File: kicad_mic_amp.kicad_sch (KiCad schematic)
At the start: 0 parts

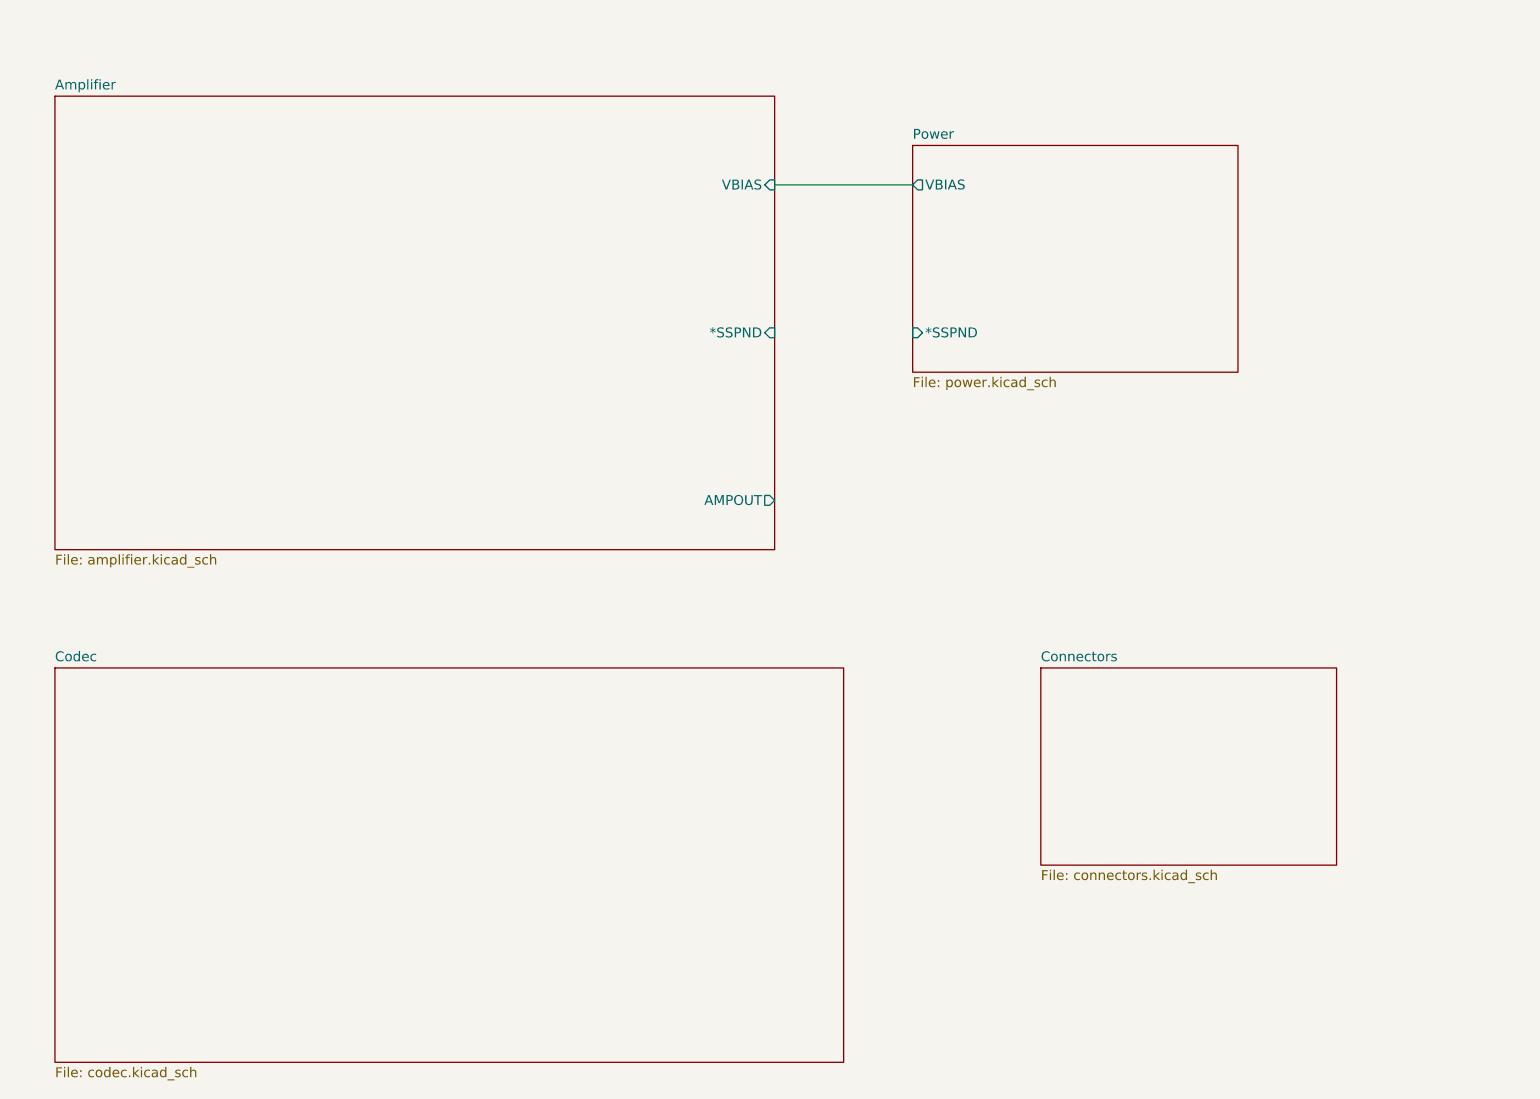
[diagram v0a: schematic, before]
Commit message: Added Connectors; added hierarchical labels connections
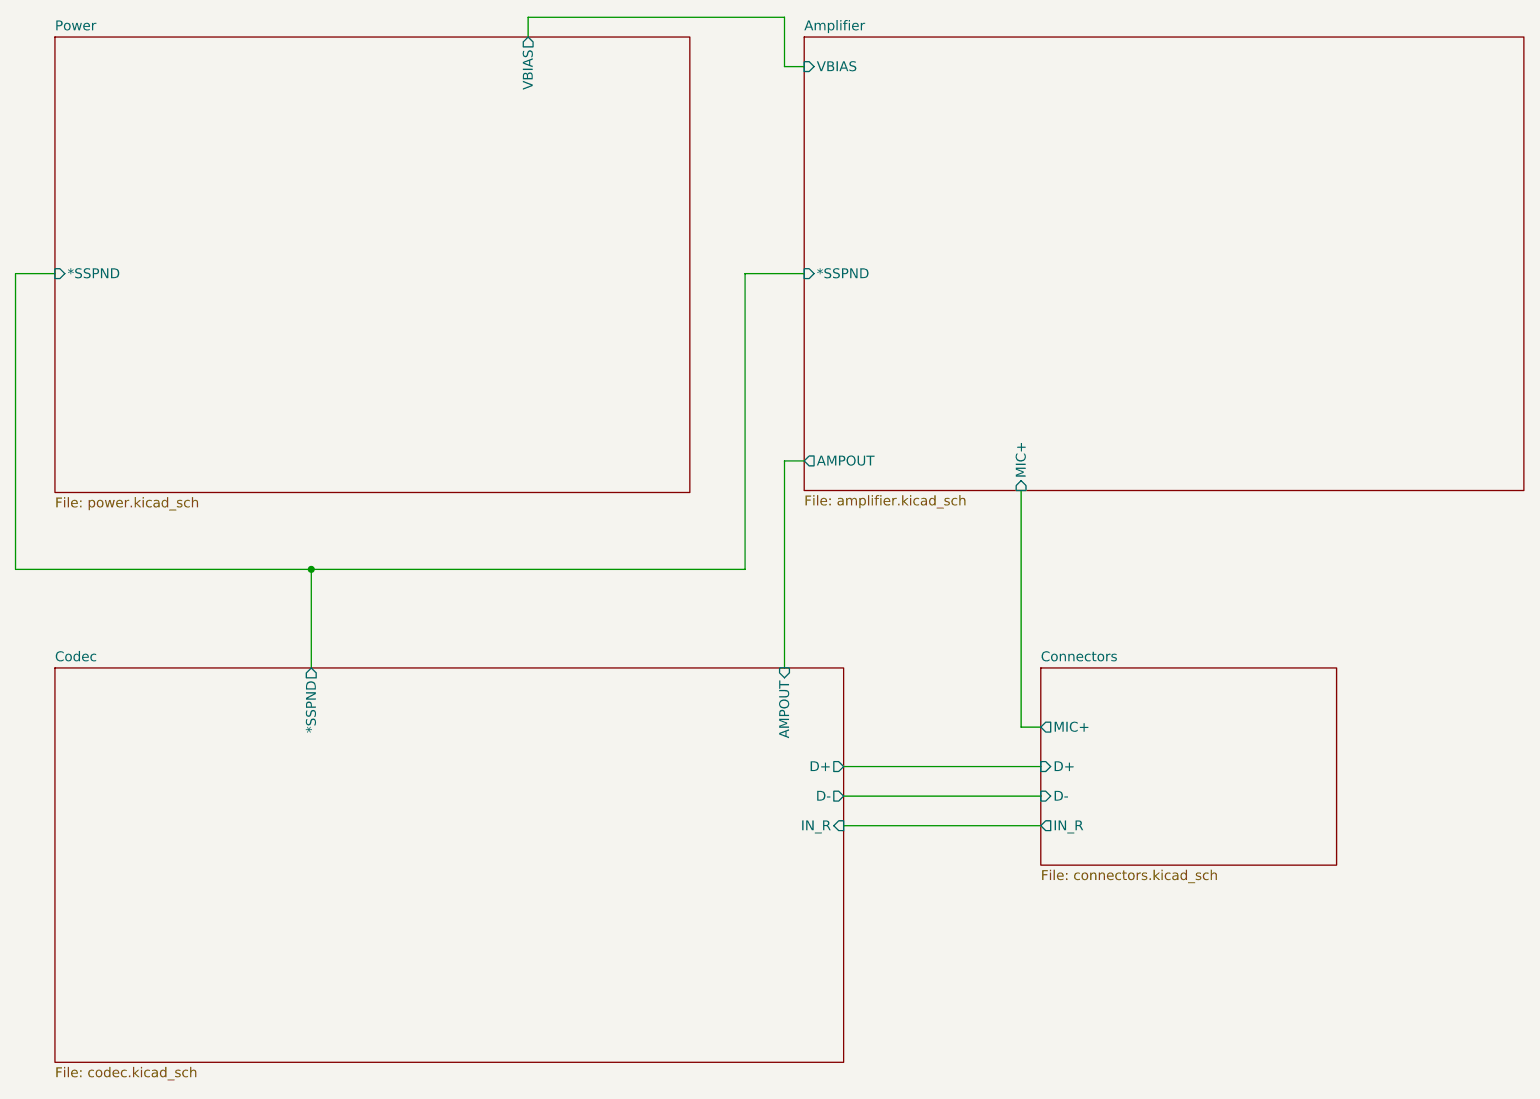
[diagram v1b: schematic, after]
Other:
- sheet Amplifier ports: added MIC+; removed none
- sheet Codec ports: added *SSPND, AMPOUT, D+, D-, IN_R; removed none
- sheet Connectors ports: added D+, D-, IN_R, MIC+; removed none

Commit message: Correct PCB; Correct Root sheet; add PCB and 3D View pictures
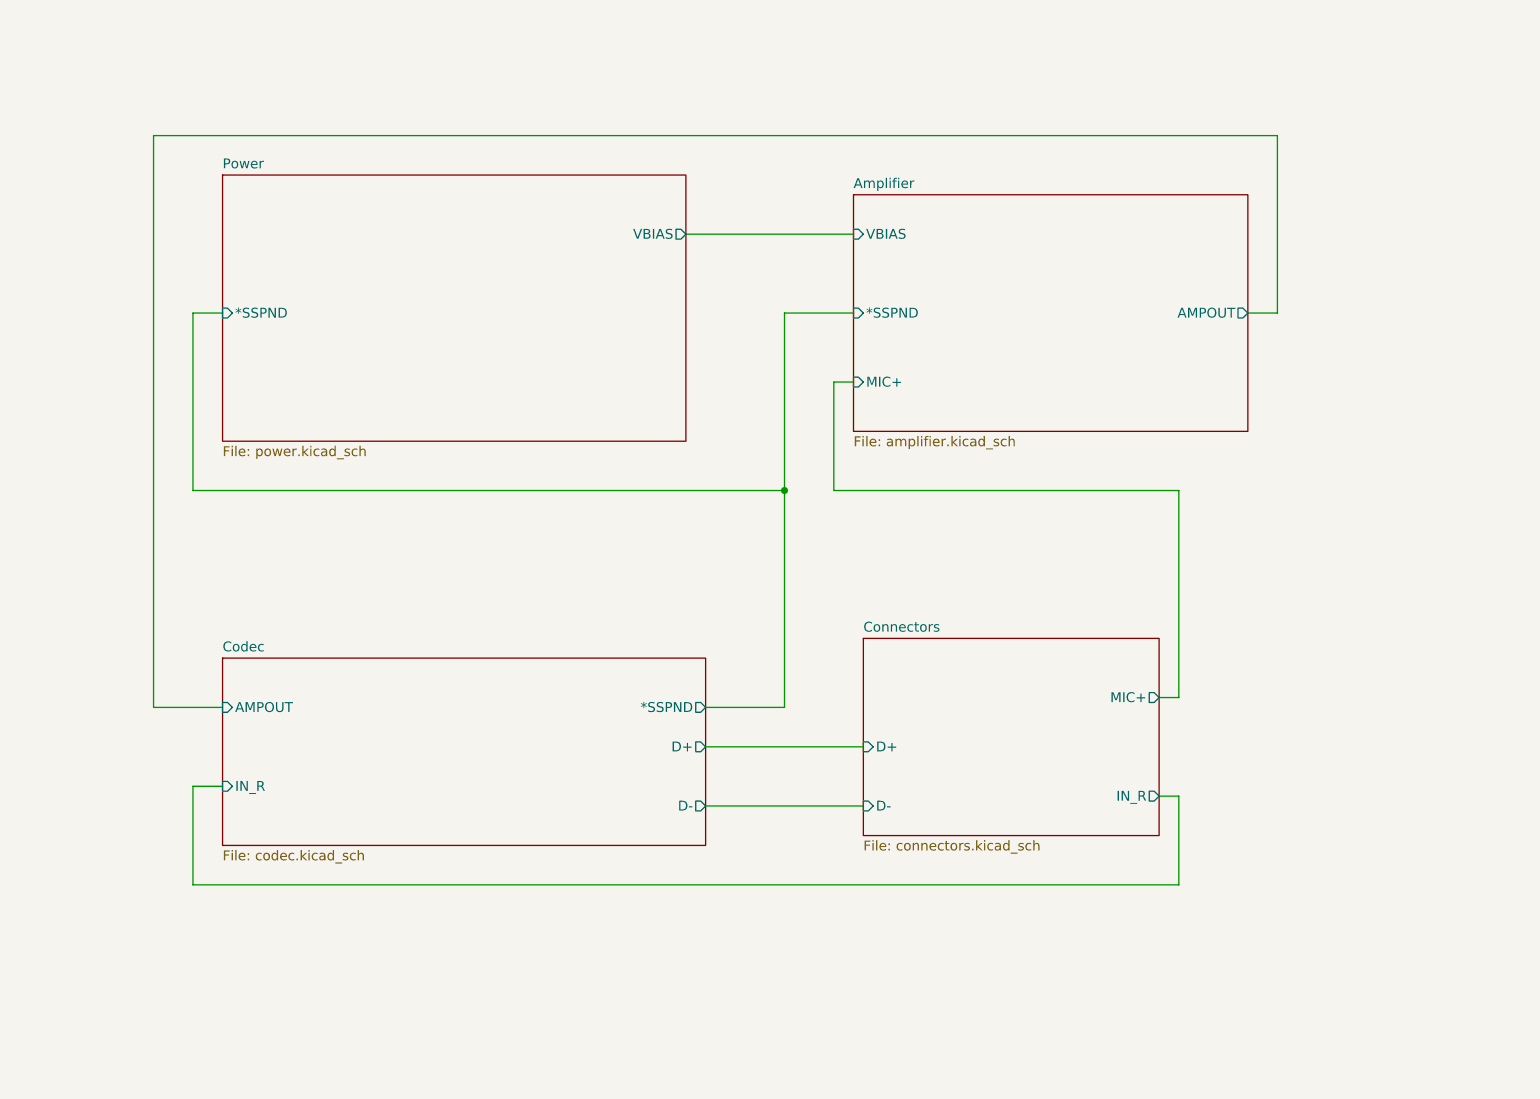
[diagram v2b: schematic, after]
